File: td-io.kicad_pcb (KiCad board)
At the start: 2 copper layers, 66.5 x 54 mm, 17 parts, among them J1 Conn_02x10_Odd_Even, J2 USB_B, J3 Conn_01x03, J4 Conn_01x02, J5 I2C, J6 DIPS, Q1 AO4818B, U1 Pico, U2 ISL3175EIBZ-T

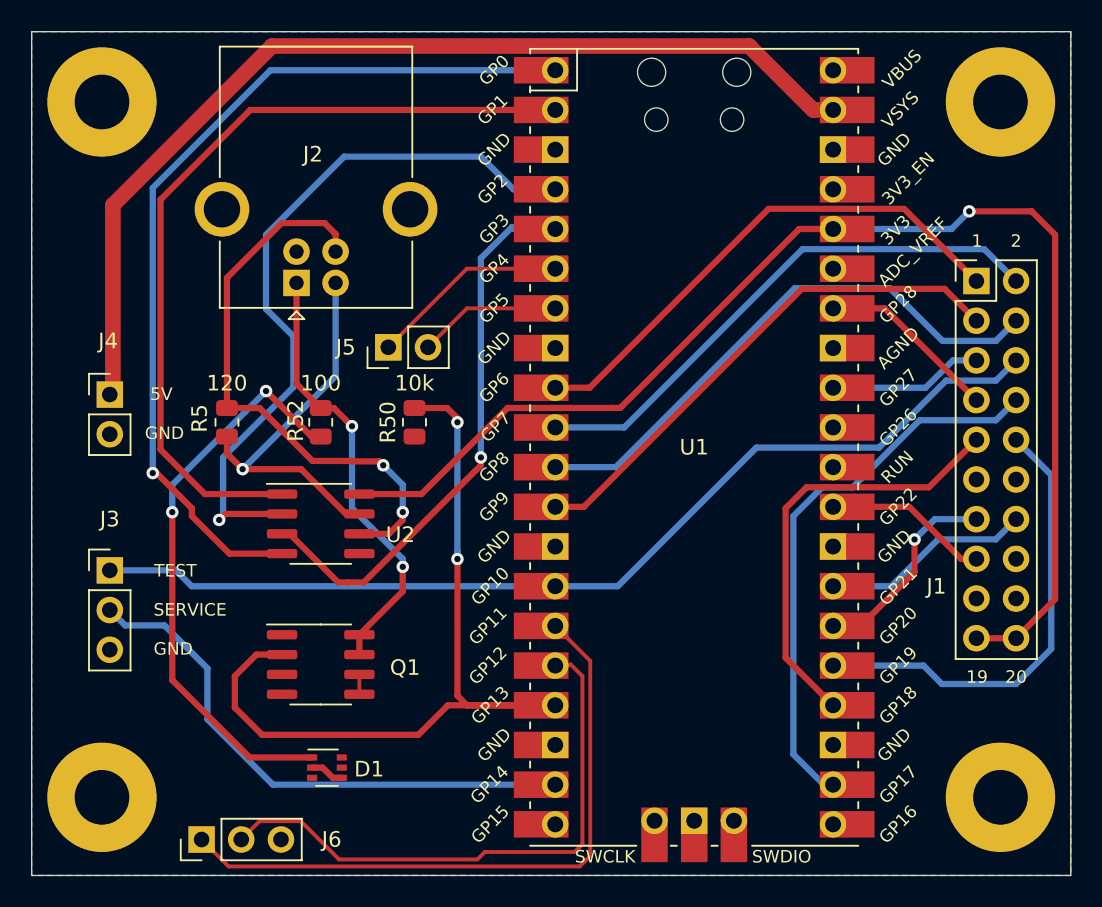
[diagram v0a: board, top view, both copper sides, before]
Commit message: Cleaned up pcb
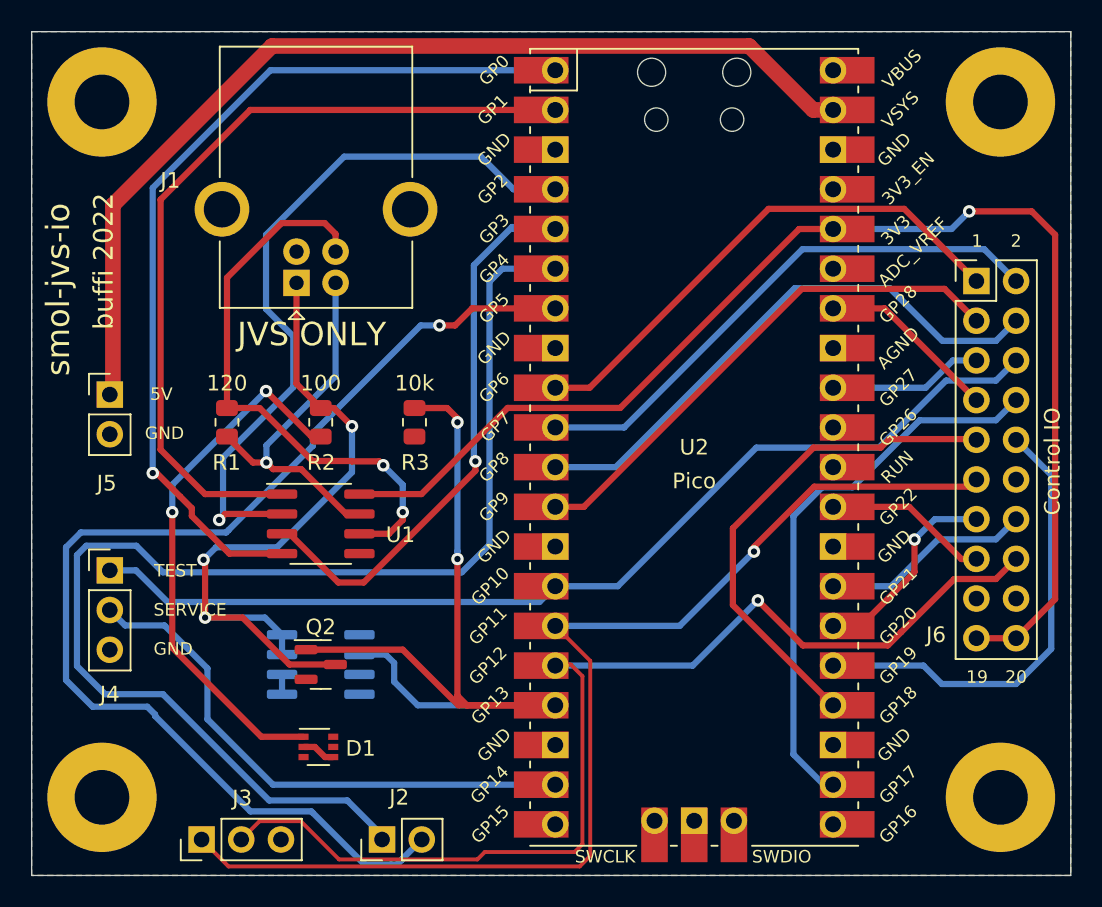
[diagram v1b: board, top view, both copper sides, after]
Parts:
- added Q2: AO3400A, Package_TO_SOT_SMD:SOT-23, F.Cu at (186.0, 84.5)
- J3: renamed from J6; value DIPS -> Dips
- J4: renamed from J3; value Conn_01x03 -> Test/Service
- J5: renamed from J4; value Conn_01x02 -> Power
- J6: renamed from J1; value Conn_02x10_Odd_Even -> Control IO
- Q1: moved to B.Cu
- moved J2 31.5 mm to (189.9, 95.7)
- moved D1 1.43 mm to (185.8, 89.8)
- turned Q1 to 180 degrees
- renumbered J2 to J1, J5 to J2, R5 to R1, R52 to R2, R50 to R3, U2 to U1, U1 to U2
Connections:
- J1 pad 1: Net-(J2-Pad1) (its old number) -> /jvs_sense
- J6 pad 11: unconnected-(J1-Pad11) -> /dip1
- J6 pad 16: unconnected-(J1-Pad16) -> /dip2
- Q1 pad 7: Net-(J2-Pad1) (its old number) -> /jvs_sense
- Q1 pad 8: Net-(J2-Pad1) (its old number) -> /jvs_sense
- R2 pad 1: Net-(J2-Pad1) (its old number) -> /jvs_sense
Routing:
- net Net-(J2-Pad1): track 12.8 -> 80.9 mm
- net Net-(J2-Pad2): track 9.18 -> 75.0 mm, vias 0 -> 1
- net /jvs_sense: track 0.00 -> 45.9 mm, vias 0 -> 3
- net /dip2: track 37.0 -> 71.3 mm, vias 0 -> 1
- net /dip1: track 41.5 -> 72.5 mm, vias 0 -> 1
- net Net-(J2-Pad1) (its old number): track 28.2 -> 0.00 mm, vias 2 -> 0
- net /sense_0v: track 54.9 -> 59.3 mm
- net /b_2: track 27.9 -> 32.0 mm
- net Net-(D1-Pad1): track 36.7 -> 34.4 mm
- net Net-(J1-Pad2): track 25.6 -> 23.9 mm
- net /b_test: track 64.4 -> 65.2 mm
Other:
- board text added: "Alternative footprint"
- board text added: "JVS ONLY"
- board text added: "buffi 2022"
- board text added: "https://github.com/buffis/smol-jvs-io"
- board text added: "smol-jvs-io"
